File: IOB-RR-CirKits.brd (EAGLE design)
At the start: 53.3 x 41.9 mm, 12 parts

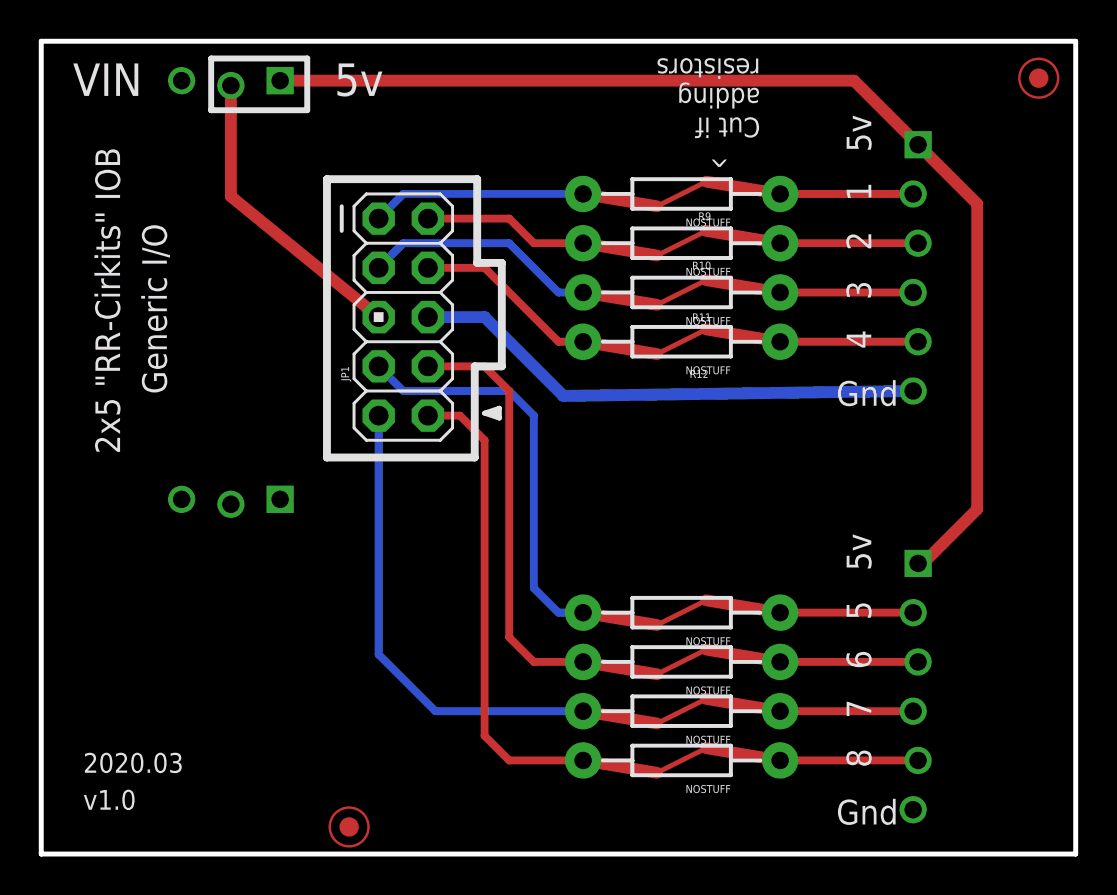
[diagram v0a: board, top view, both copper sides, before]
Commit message: added 2-up array
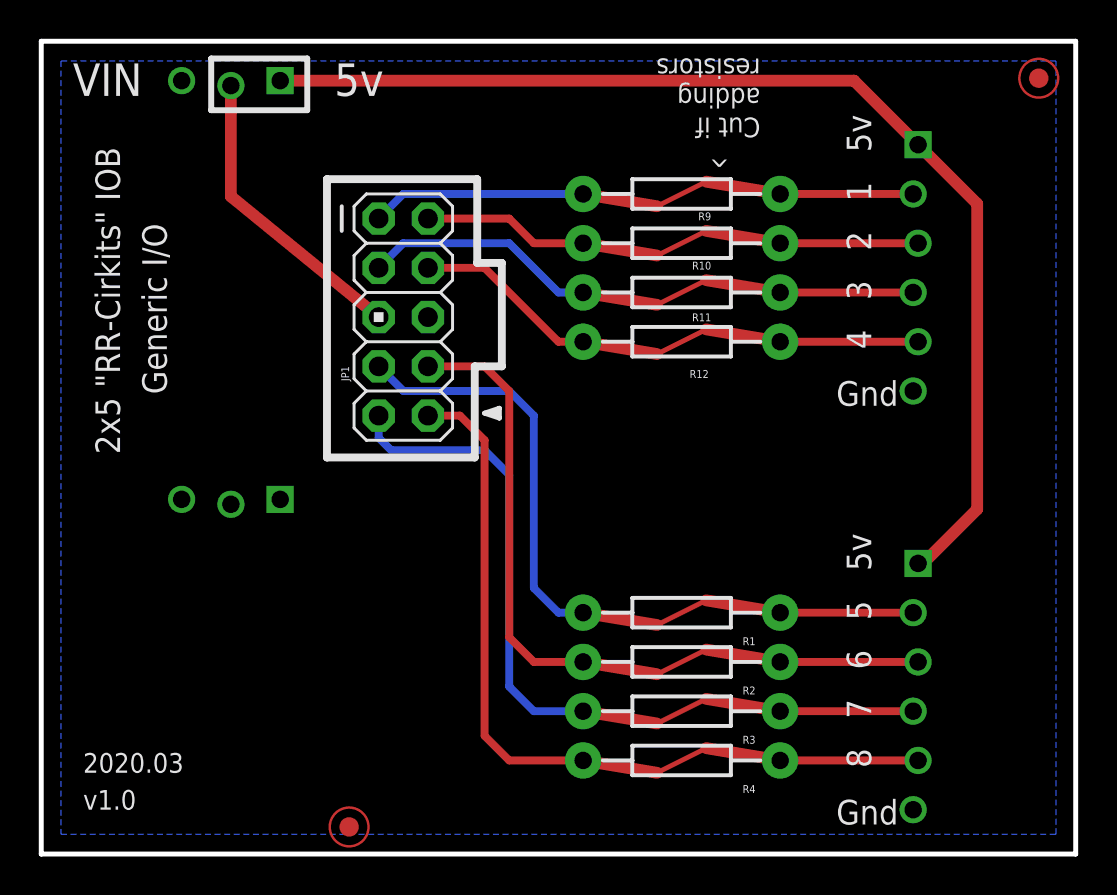
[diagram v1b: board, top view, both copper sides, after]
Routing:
- net GND: track 26.7 -> 0.00 mm
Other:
- board text added: "JP1"
- board text added: "R1"
- board text added: "R12"
- board text added: "R2"
- board text added: "R3"
- board text added: "R4"

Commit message: normalized silkscreen layout across IOBs
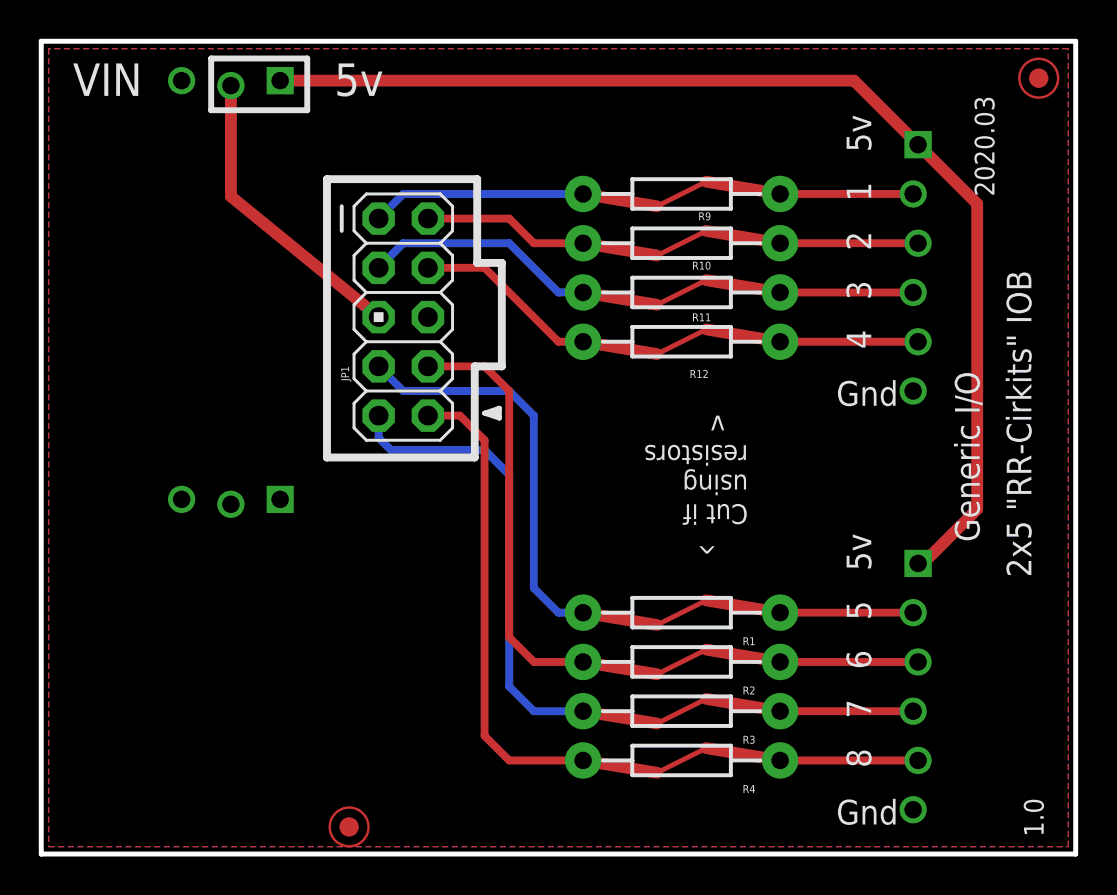
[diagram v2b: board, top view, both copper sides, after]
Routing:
- added copper zone on layer 1, net VCC
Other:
- board text added: "1.0"
- board text added: "Yellow Headers"
- board text added: "Yellow Soldermask White Silkscreen"
- board text added: "^ Cut if using resistors v"
- board text removed: "Yellow Soldermask Black Silkscreen"
- board text removed: "^ Cut if adding resistors"
- board text removed: "v1.0"
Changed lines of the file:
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@@
 <setting verticaltext="up"/>
 </settings>
-<grid distance="50" unitdist="mil" unit="mil" style="dots" multiple="2" display="yes" altdistance="5" altunitdist="mil" altunit="mil"/>
+<grid distance="50" unitdist="mil" unit="mil" style="dots" multiple="2" display="yes" altdistance="25" altunitdist="mil" altunit="mil"/>
 <layers>
 <layer number="1" name="Top" color="4" fill="1" visible="yes" active="yes"/>
@@
 <layer number="20" name="Dimension" color="15" fill="1" visible="yes" active="yes"/>
 <layer number="21" name="tPlace" color="35" fill="1" visible="yes" active="yes"/>
-<layer number="22" name="bPlace" color="17" fill="1" visible="no" active="yes"/>
+<layer number="22" name="bPlace" color="17" fill="1" visible="yes" active="yes"/>
 <layer number="23" name="tOrigins" color="30" fill="1" visible="yes" active="yes"/>
-<layer number="24" name="bOrigins" color="15" fill="1" visible="no" active="yes"/>
+<layer number="24" name="bOrigins" color="15" fill="1" visible="yes" active="yes"/>
 <layer number="25" name="tNames" color="63" fill="1" visible="yes" active="yes"/>
-<layer number="26" name="bNames" color="34" fill="1" visible="no" active="yes"/>
+<layer number="26" name="bNames" color="34" fill="1" visible="yes" active="yes"/>
 <layer number="27" name="tValues" color="56" fill="1" visible="yes" active="yes"/>
-<layer number="28" name="bValues" color="7" fill="1" visible="no" active="yes"/>
-<layer number="29" name="tStop" color="7" fill="3" visible="no" active="yes"/>
-<layer number="30" name="bStop" color="7" fill="6" visible="no" active="yes"/>
-<layer number="31" name="tCream" color="7" fill="4" visible="no" active="yes"/>
-<layer number="32" name="bCream" color="7" fill="5" visible="no" active="yes"/>
-<layer number="33" name="tFinish" color="6" fill="3" visible="no" active="yes"/>
-<layer number="34" name="bFinish" color="6" fill="6" visible="no" active="yes"/>
-<layer number="35" name="tGlue" color="7" fill="4" visible="no" active="yes"/>
-<layer number="36" name="bGlue" color="7" fill="5" visible="no" active="yes"/>
-<layer number="37" name="tTest" color="7" fill="1" visible="no" active="yes"/>
-<layer number="38" name="bTest" color="7" fill="1" visible="no" active="yes"/>
-<layer number="39" name="tKeepout" color="4" fill="11" visible="no" active="yes"/>
-<layer number="40" name="bKeepout" color="3" fill="11" visible="no" active="yes"/>
-<layer number="41" name="tRestrict" color="4" fill="10" visible="no" active="yes"/>
-<layer number="42" name="bRestrict" color="3" fill="10" visible="no" active="yes"/>
-<layer number="43" name="vRestrict" color="2" fill="10" visible="no" active="yes"/>
+<layer number="28" name="bValues" color="7" fill="1" visible="yes" active="yes"/>
+<layer number="29" name="tStop" color="7" fill="3" visible="yes" active="yes"/>
+<layer number="30" name="bStop" color="7" fill="6" visible="yes" active="yes"/>
+<layer number="31" name="tCream" color="7" fill="4" visible="yes" active="yes"/>
+<layer number="32" name="bCream" color="7" fill="5" visible="yes" active="yes"/>
+<layer number="33" name="tFinish" color="6" fill="3" visible="yes" active="yes"/>
+<layer number="34" name="bFinish" color="6" fill="6" visible="yes" active="yes"/>
+<layer number="35" name="tGlue" color="7" fill="4" visible="yes" active="yes"/>
+<layer number="36" name="bGlue" color="7" fill="5" visible="yes" active="yes"/>
+<layer number="37" name="tTest" color="7" fill="1" visible="yes" active="yes"/>
+<layer number="38" name="bTest" color="7" fill="1" visible="yes" active="yes"/>
+<layer number="39" name="tKeepout" color="4" fill="11" visible="yes" active="yes"/>
+<layer number="40" name="bKeepout" color="3" fill="11" visible="yes" active="yes"/>
+<layer number="41" name="tRestrict" color="4" fill="10" visible="yes" active="yes"/>
+<layer number="42" name="bRestrict" color="3" fill="10" visible="yes" active="yes"/>
+<layer number="43" name="vRestrict" color="2" fill="10" visible="yes" active="yes"/>
 <layer number="44" name="Drills" color="16" fill="1" visible="yes" active="yes"/>
 <layer number="45" name="Holes" color="35" fill="1" visible="yes" active="yes"/>
@@
 <layer number="48" name="Document" color="57" fill="1" visible="yes" active="yes"/>
 <layer number="49" name="Reference" color="48" fill="1" visible="yes" active="yes"/>
-<layer number="50" name="dxf" color="7" fill="1" visible="no" active="yes"/>
+<layer number="50" name="dxf" color="7" fill="1" visible="yes" active="yes"/>
 <layer number="51" name="tDocu" color="8" fill="1" visible="yes" active="yes"/>
-<layer number="52" name="bDocu" color="7" fill="1" visible="no" active="yes"/>
+<layer number="52" name="bDocu" color="7" fill="1" visible="yes" active="yes"/>
 <layer number="91" name="Nets" color="2" fill="1" visible="no" active="no"/>
 <layer number="92" name="Busses" color="1" fill="1" visible="no" active="no"/>
@@
 <board>
 <plain>
-<text x="2.794" y="36.449" size="1.27" layer="21" font="vector" rot="R270">2x5 "RR-Cirkits" IOB</text>
-<text x="2.159" y="2.286" size="1.016" layer="21" font="vector">v1.0</text>
-<text x="5.207" y="32.512" size="1.27" layer="21" font="vector" rot="R270">Generic I/O</text>
+<text x="49.784" y="30.099" size="1.27" layer="21" font="vector" rot="R270">2x5 "RR-Cirkits" IOB</text>
+<text x="51.689" y="0.889" size="1.016" layer="21" font="vector" rot="R90">1.0</text>
+<text x="47.117" y="24.892" size="1.27" layer="21" font="vector" rot="R270">Generic I/O</text>
 <text x="3.683" y="35.814" size="1.27" layer="22" font="vector" rot="MR270">John Plocher</text>
 <text x="40.005" y="14.986" size="1.4224" layer="22" font="vector" rot="MR0">RR-Cirkits-compatible 8-bit I/O</text>
-<text x="0" y="43.18" size="1.778" layer="48" font="vector" ratio="10">Yellow Soldermask
-Black Silkscreen</text>
-<text x="37.084" y="41.021" size="1.016" layer="21" font="vector" ratio="10" rot="SR180">    ^
+<text x="-1.27" y="10.16" size="1.778" layer="48" font="vector" ratio="10" rot="R90">Yellow Soldermask
+White Silkscreen</text>
+<text x="36.449" y="22.606" size="1.016" layer="21" font="vector" ratio="10" rot="SR180">    ^
 Cut if
-adding
-resistors</text>
-<text x="2.159" y="4.191" size="1.016" layer="21" font="vector">2020.03</text>
+using
+resistors
+   v</text>
+<text x="49.149" y="33.909" size="1.016" layer="21" font="vector" rot="R90">2020.03</text>
 <wire x1="14.732" y1="34.798" x2="22.479" y2="34.798" width="0.4064" layer="21"/>
 <wire x1="22.479" y1="34.798" x2="22.479" y2="30.48" width="0.4064" layer="21"/>
@@
 <wire x1="23.622" y1="22.987" x2="23.622" y2="22.479" width="0.254" layer="21"/>
 <wire x1="22.987" y1="22.733" x2="23.495" y2="22.733" width="0.254" layer="21"/>
+<rectangle x1="29.21" y1="24.13" x2="36.83" y2="36.195" layer="41"/>
+<rectangle x1="29.21" y1="2.54" x2="36.83" y2="14.605" layer="41"/>
+<text x="55.88" y="10.16" size="1.778" layer="48" font="vector" ratio="10" rot="R90">Yellow Headers</text>
 <text x="15.875" y="24.384" size="0.4064" layer="125" font="vector" rot="R90">JP1</text>
 <text x="36.83" y="11.176" size="0.4064" layer="125" font="vector" rot="R180">R1</text>
@@
 <contactref element="JP1" pad="6"/>
 <polygon width="0.3048" layer="16" isolate="0.4064">
-<vertex x="1.016" y="40.894"/>
-<vertex x="1.016" y="1.016"/>
-<vertex x="52.324" y="1.016"/>
-<vertex x="52.324" y="40.894"/>
+<vertex x="0.381" y="41.529"/>
+<vertex x="0.381" y="0.381"/>
+<vertex x="52.959" y="0.381"/>
+<vertex x="52.959" y="41.529"/>
 </polygon>
 </signal>
@@
 <wire x1="48.26" y1="17.78" x2="45.466" y2="14.986" width="0.6096" layer="1"/>
 <wire x1="45.466" y1="14.986" x2="45.212" y2="14.986" width="0.6096" layer="1"/>
-<wire x1="12.319" y1="18.288" x2="12.319" y2="39.878" width="0" layer="19" extent="1-1"/>
+<polygon width="0.3048" layer="1" isolate="0.4064">
+<vertex x="0.381" y="41.529"/>
+<vertex x="0.381" y="0.381"/>
+<vertex x="52.959" y="0.381"/>
+<vertex x="52.959" y="41.529"/>
+</polygon>
 </signal>
 <signal name="VCCIO">
